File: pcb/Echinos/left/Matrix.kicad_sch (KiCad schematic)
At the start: 48 parts, among them SW200 SW_Push, SW201 SW_Push, SW202 SW_Push, SW203 SW_Push, SW204 SW_Push, SW205 SW_Push, SW206 SW_Push, SW207 SW_Push, SW208 SW_Push, SW209 SW_Push, SW210 SW_Push, SW211 SW_Push, SW212 SW_Push, SW213 SW_Push, SW214 SW_Push, SW215 SW_Push, SW216 SW_Push, SW217 SW_Push, SW218 SW_Push, SW219 SW_Push, SW220 SW_Push, SW221 SW_Push, SW222 SW_Push, SW223 SW_Push

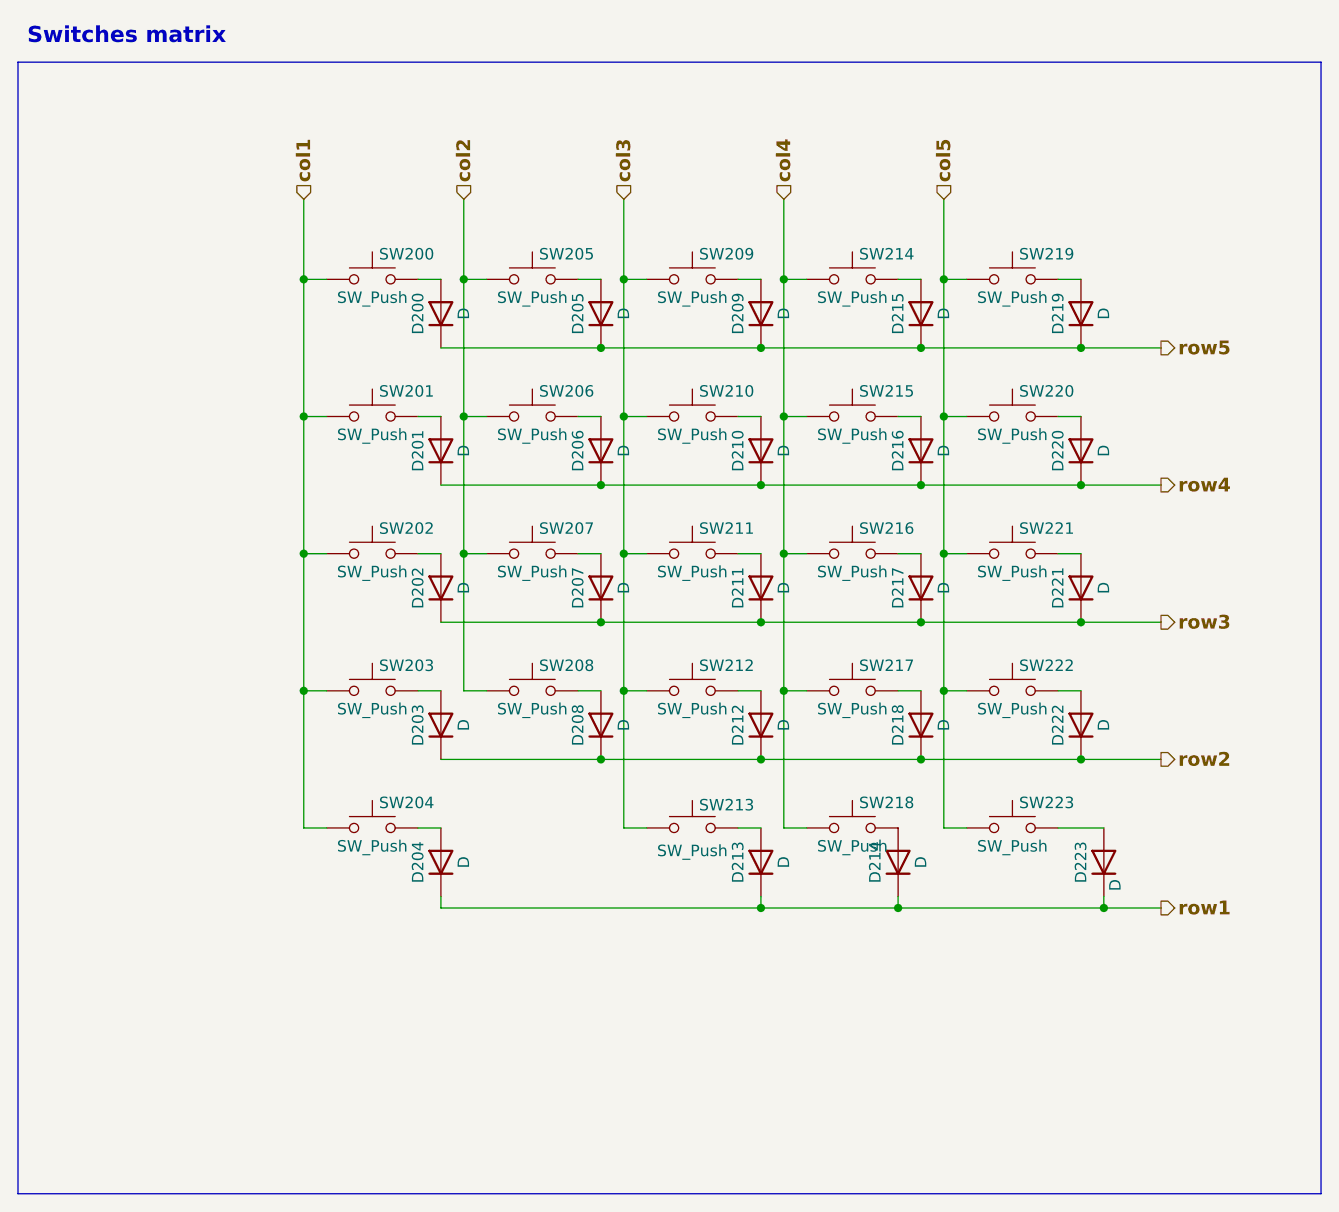
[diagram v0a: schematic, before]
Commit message: 💥 [PCB] - Split schematic for left and right halves.   - Required to create a common PCB to lower the manufacturing cost
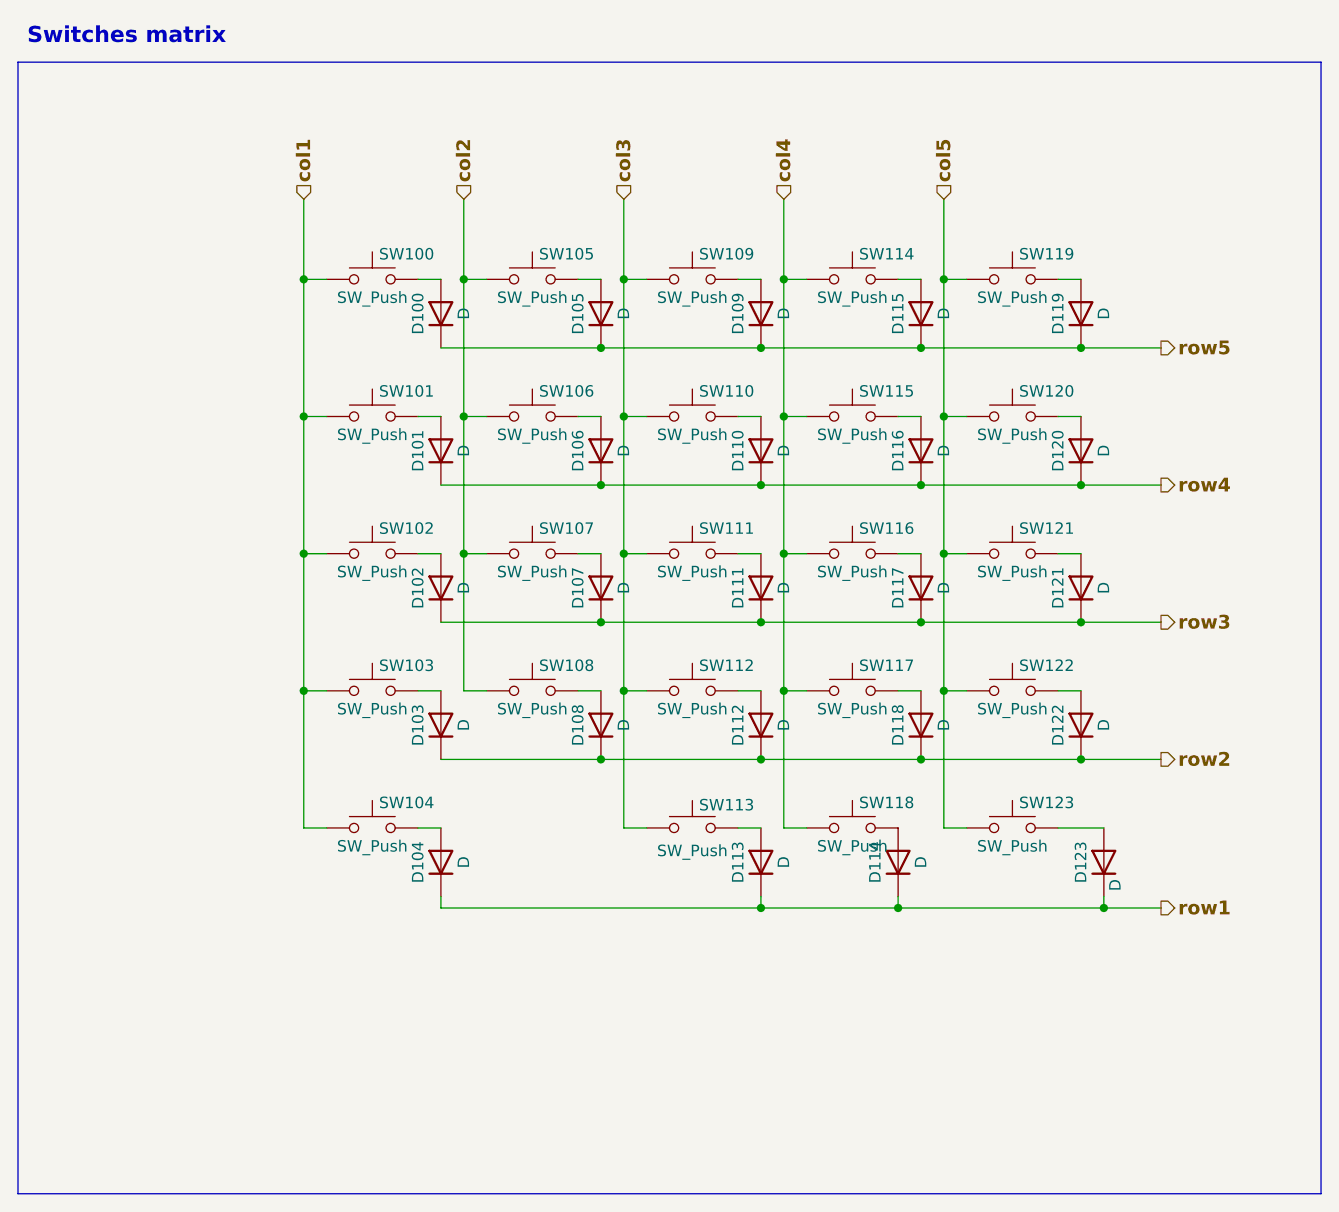
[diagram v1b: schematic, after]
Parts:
- renumbered D200 to D100, D201 to D101, D202 to D102, D203 to D103, D204 to D104, D205 to D105, D206 to D106, D207 to D107, D208 to D108, D209 to D109, D210 to D110, D211 to D111, D212 to D112, D213 to D113, D214 to D114, D215 to D115, D216 to D116, D217 to D117, D218 to D118, D219 to D119, D220 to D120, D221 to D121, D222 to D122, D223 to D123, SW200 to SW100, SW201 to SW101, SW202 to SW102, SW203 to SW103, SW204 to SW104, SW205 to SW105, SW206 to SW106, SW207 to SW107, SW208 to SW108, SW209 to SW109, SW210 to SW110, SW211 to SW111, SW212 to SW112, SW213 to SW113, SW214 to SW114, SW215 to SW115, SW216 to SW116, SW217 to SW117, SW218 to SW118, SW219 to SW119, SW220 to SW120, SW221 to SW121, SW222 to SW122, SW223 to SW123

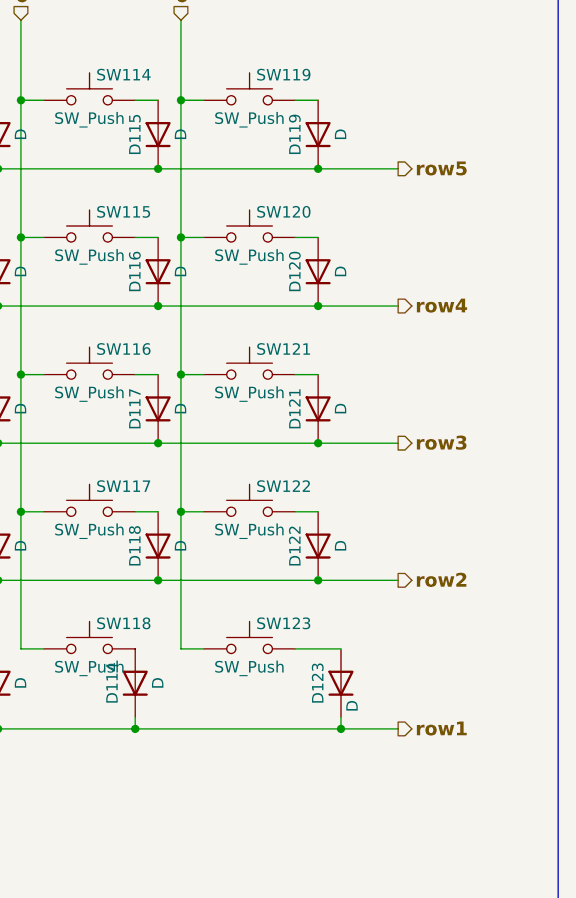
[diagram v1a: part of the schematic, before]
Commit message: 💥 [PCB] - Group left and right on the same PCB.   - Schematics are different for each side   - Split trace naming to avoid mixing right and left   - Add mouse bite between both halves to make manufacturing easier (new footprint)
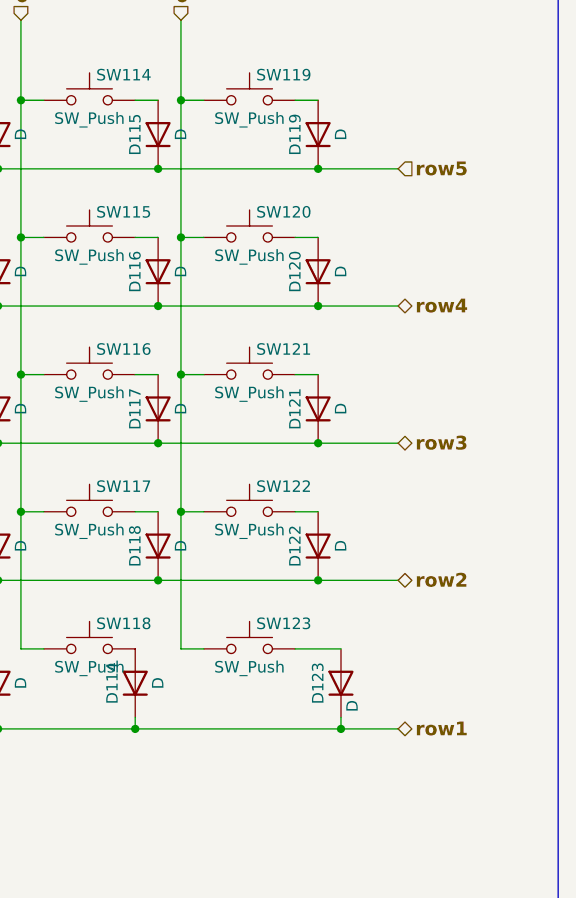
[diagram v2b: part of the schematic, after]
